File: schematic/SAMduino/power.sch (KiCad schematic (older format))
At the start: 35 parts, among them IC2 MCP1703AT-5002E_CB, IC3 NCP5501DT33RKG, J1 Barrel_Jack_Switch, J2 Conn_02x02_Odd_Even, J3 USB_B_Micro, J4 USB_B_Mini

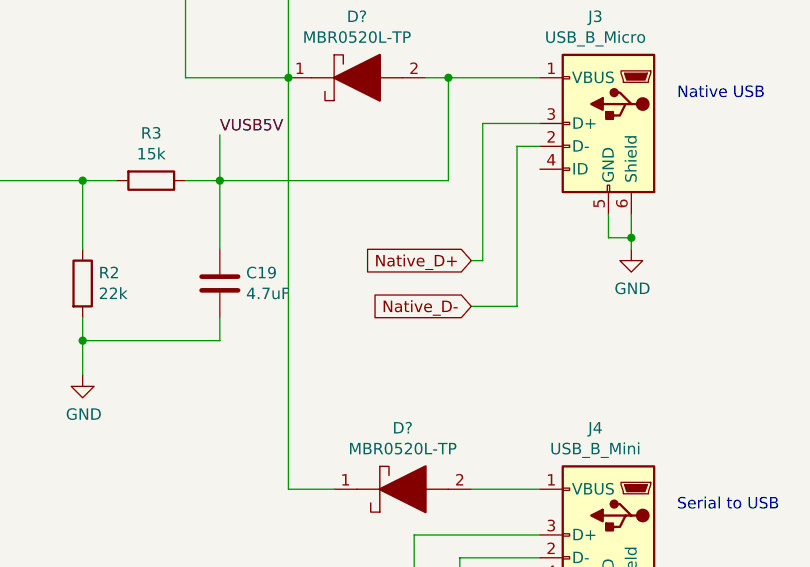
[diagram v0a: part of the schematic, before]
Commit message: Specialty pins wired
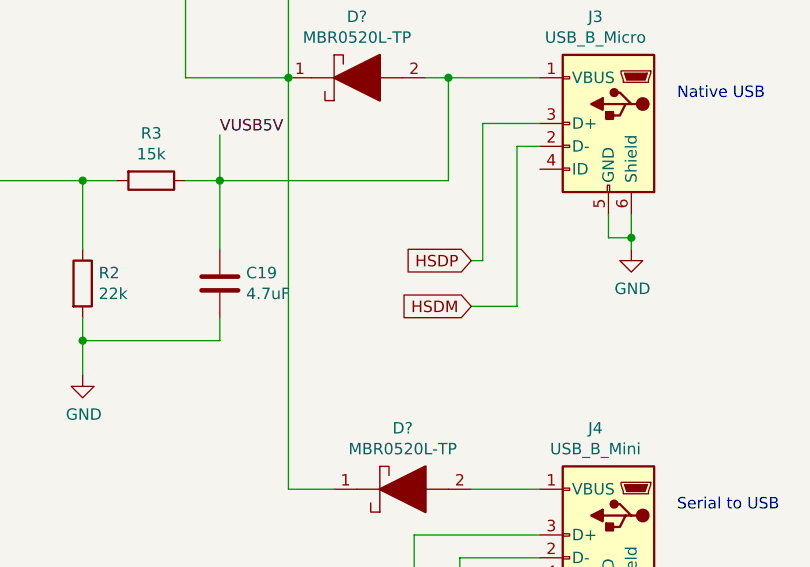
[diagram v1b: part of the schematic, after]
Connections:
- net Native_D+ renamed HSDP
- net Native_D- renamed HSDM
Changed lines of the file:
@@
 Serial_D-
 Text GLabel 7500 2250 0    50   Input ~ 0
-Native_D+
+HSDP
 Text GLabel 7500 2450 0    50   Input ~ 0
-Native_D-
+HSDM
 Wire Wire Line
 	7050 3750 7250 3750

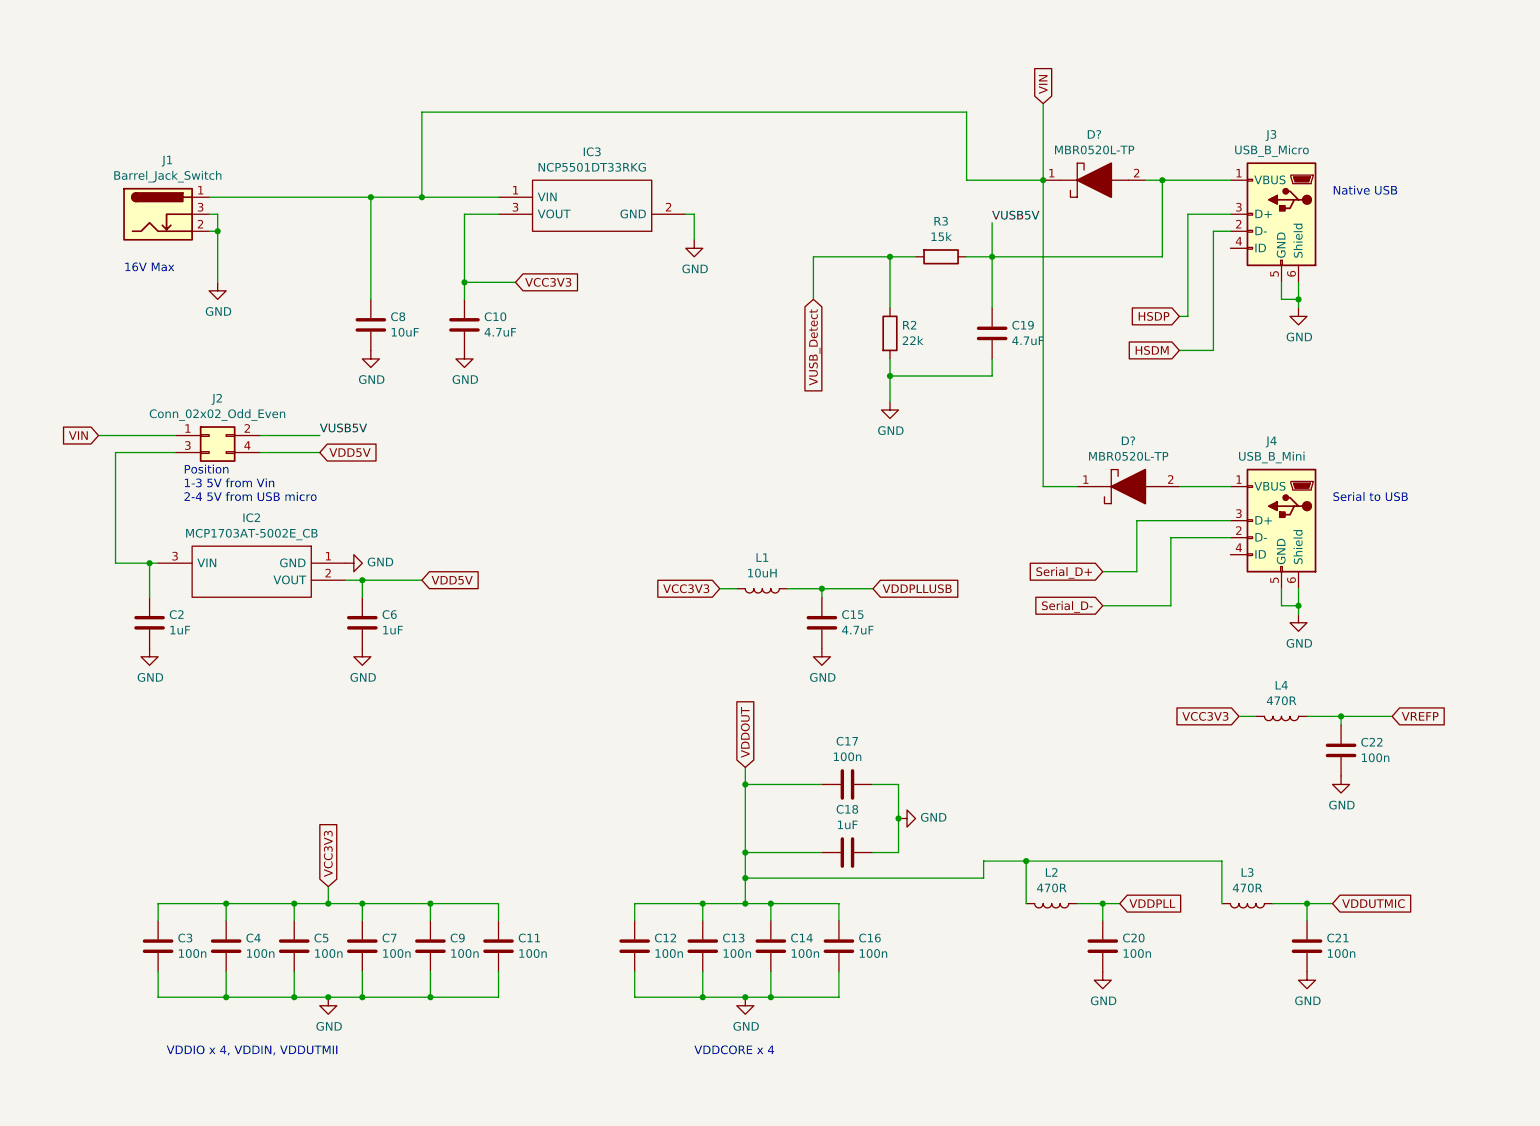
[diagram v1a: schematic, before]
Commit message: All pins connected
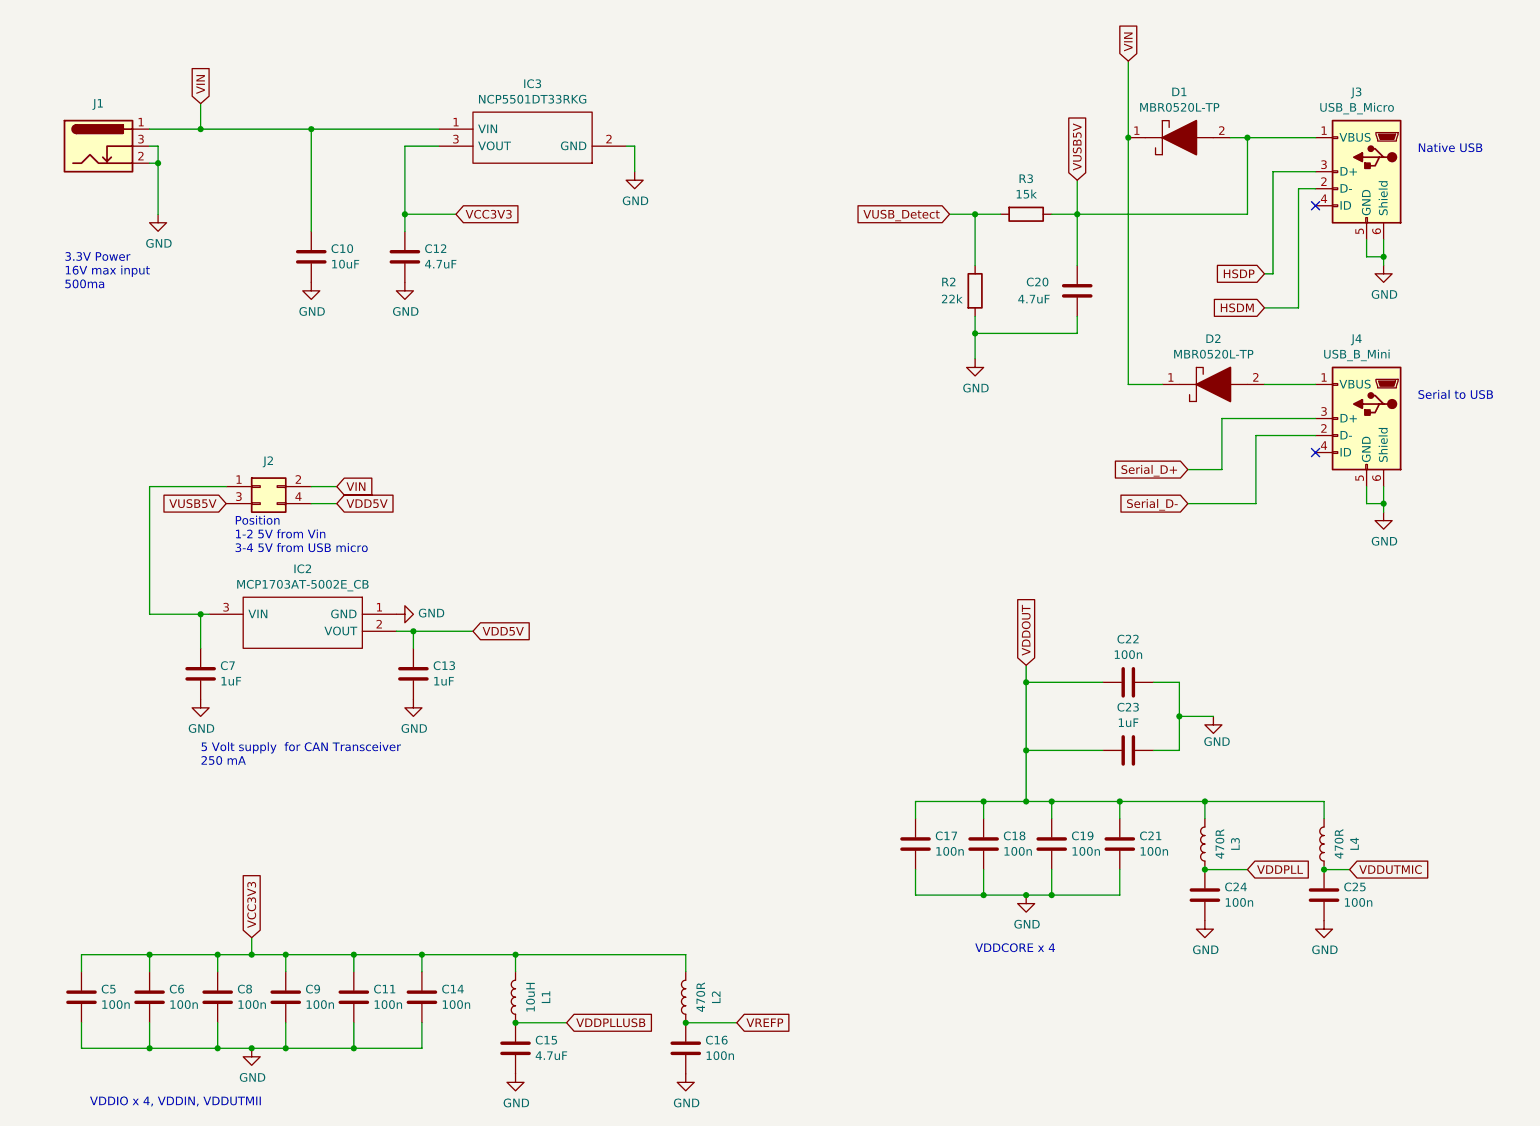
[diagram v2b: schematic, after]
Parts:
- gave numbers to parts that had none: 2
- renumbered C8 to C10, C9 to C11, C10 to C12, C6 to C13, C11 to C14, C22 to C16, C12 to C17, C13 to C18, C14 to C19, C19 to C20, C16 to C21, C17 to C22, C18 to C23, C20 to C24, C21 to C25, C3 to C5, C4 to C6, C2 to C7, C5 to C8, C7 to C9, L4 to L2, L2 to L3, L3 to L4
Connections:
- net VIN: now also J2.2 (Pin_2); no longer J2.1 (Pin_1)
- net VUSB5V: now also J2.3 (Pin_3); no longer J2.2 (Pin_2)
- net at C7.1, IC2.3 (VIN): now also J2.1 (Pin_1); no longer J2.3 (Pin_3)
- no-connect marks 0 -> 2
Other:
- note added: "3.3V Power\n16V max input\n500ma"
- note added: "5 Volt supply for CAN Transceiver\n250 mA"
- note added: "Position\n1-2 5V from Vin\n3-4 5V from USB micro"
- note removed: "16V Max"
- note removed: "Position\n1-3 5V from Vin\n2-4 5V from USB micro"
- moved on the sheet: C10, C11, C12, C13, C14, C15, C16, C17, C18, C19, C20, C21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

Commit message: Schematic with footprints
Some footprints need to be verified with actual components
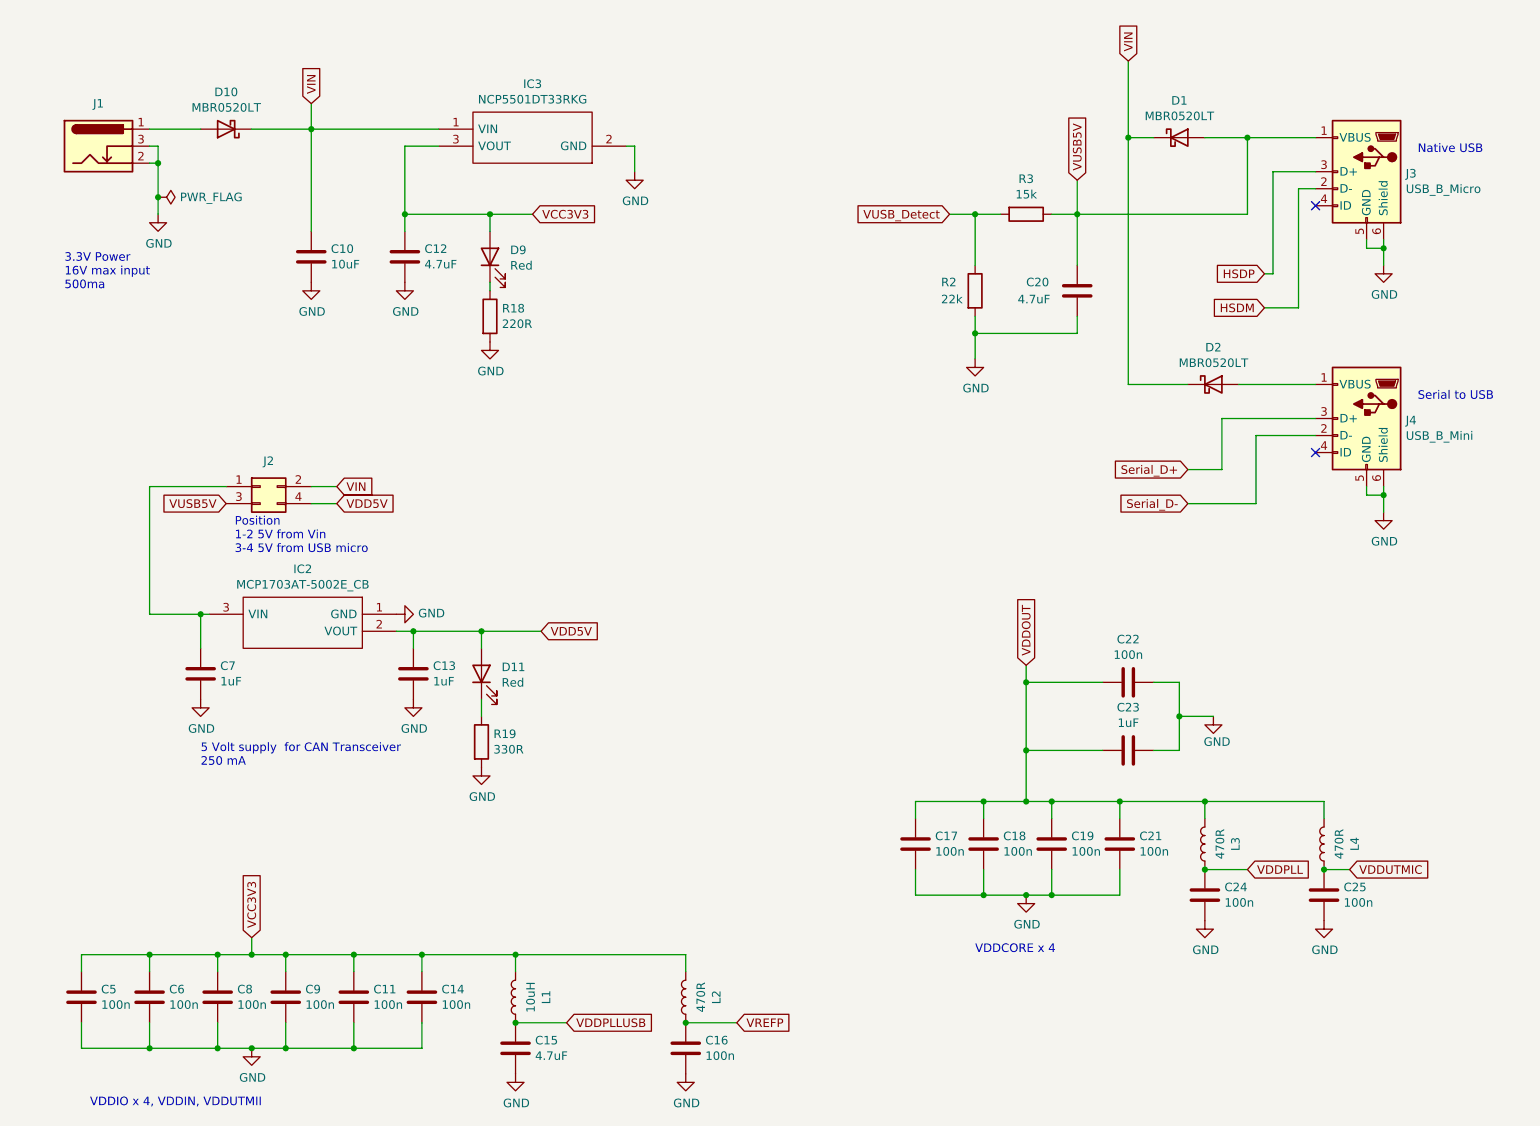
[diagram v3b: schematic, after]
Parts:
- removed D1, D2: MBR0520L-TP, SOD3716X135N, symbol SamacSys_Parts:MBR0520L-TP
- removed J3: USB_B_Micro, symbol Connector:USB_B_Micro
- removed J4: USB_B_Mini, symbol Connector:USB_B_Mini
- added D1, D10, D2: MBR0520LT, Diode_SMD:D_SOD-123, symbol Diode:MBR0520LT
- added D11, D9: Red, LED_SMD:LED_0603_1608Metric, symbol Device:LED
- added J3: USB_B_Micro, Connector_USB:USB_Micro-B_Amphenol_10104110_Horizontal, symbol SamacSys_Parts:USB_B_Micro
- added J4: USB_B_Mini, Connector_USB:USB_Mini-B_Wuerth_65100516121_Horizontal, symbol SamacSys_Parts:USB_B_Mini
- added R18: 220R, Resistor_SMD:R_0603_1608Metric, symbol Device:R
- added R19: 330R, Resistor_SMD:R_0603_1608Metric, symbol Device:R
- C10, C12, C13, C15, C20, C7: footprint (none) -> Capacitor_SMD:C_0603_1608Metric
- C11, C14, C16, C17, C18, C19, C21, C22, C23, C24, C25, C5, C6, C8, C9: footprint (none) -> Capacitor_SMD:C_0402_1005Metric
- IC2: footprint SOT95P255X145-3N -> SamacSys_Parts:SOT95P255X145-3N
- IC3: footprint NVD5117PLT4GVF01 -> SamacSys_Parts:NVD5117PLT4GVF01
- J1: footprint (none) -> Connector_BarrelJack:BarrelJack_Wuerth_6941xx301002
- J2: footprint (none) -> Connector_PinHeader_2.54mm:PinHeader_2x02_P2.54mm_Vertical
- L1, L2, L3, L4: footprint (none) -> Inductor_SMD:L_0603_1608Metric
- R2, R3: footprint (none) -> Resistor_SMD:R_0603_1608Metric
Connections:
- net GND: now also J3.5 (GND), J3.6 (Shield), J4.5 (GND), J4.6 (Shield), R18.2, R19.2
- net HSDM: now also J3.2 (D-)
- net HSDP: now also J3.3 (D+)
- net Serial_D+: now also J4.3 (D+)
- net Serial_D-: now also J4.2 (D-)
- net VCC3V3: now also D9.2 (A)
- net VDD5V: now also D11.2 (A)
- net VIN: now also D1.1 (K), D10.1 (K), D2.1 (K); no longer J1.1
- net VUSB5V: now also D1.2 (A), J3.1 (VBUS)
- new net: D10.2 (A), J1.1
- new net: D9.1 (K), R18.1
- new net: D2.2 (A), J4.1 (VBUS)
- new net: D11.1 (K), R19.1

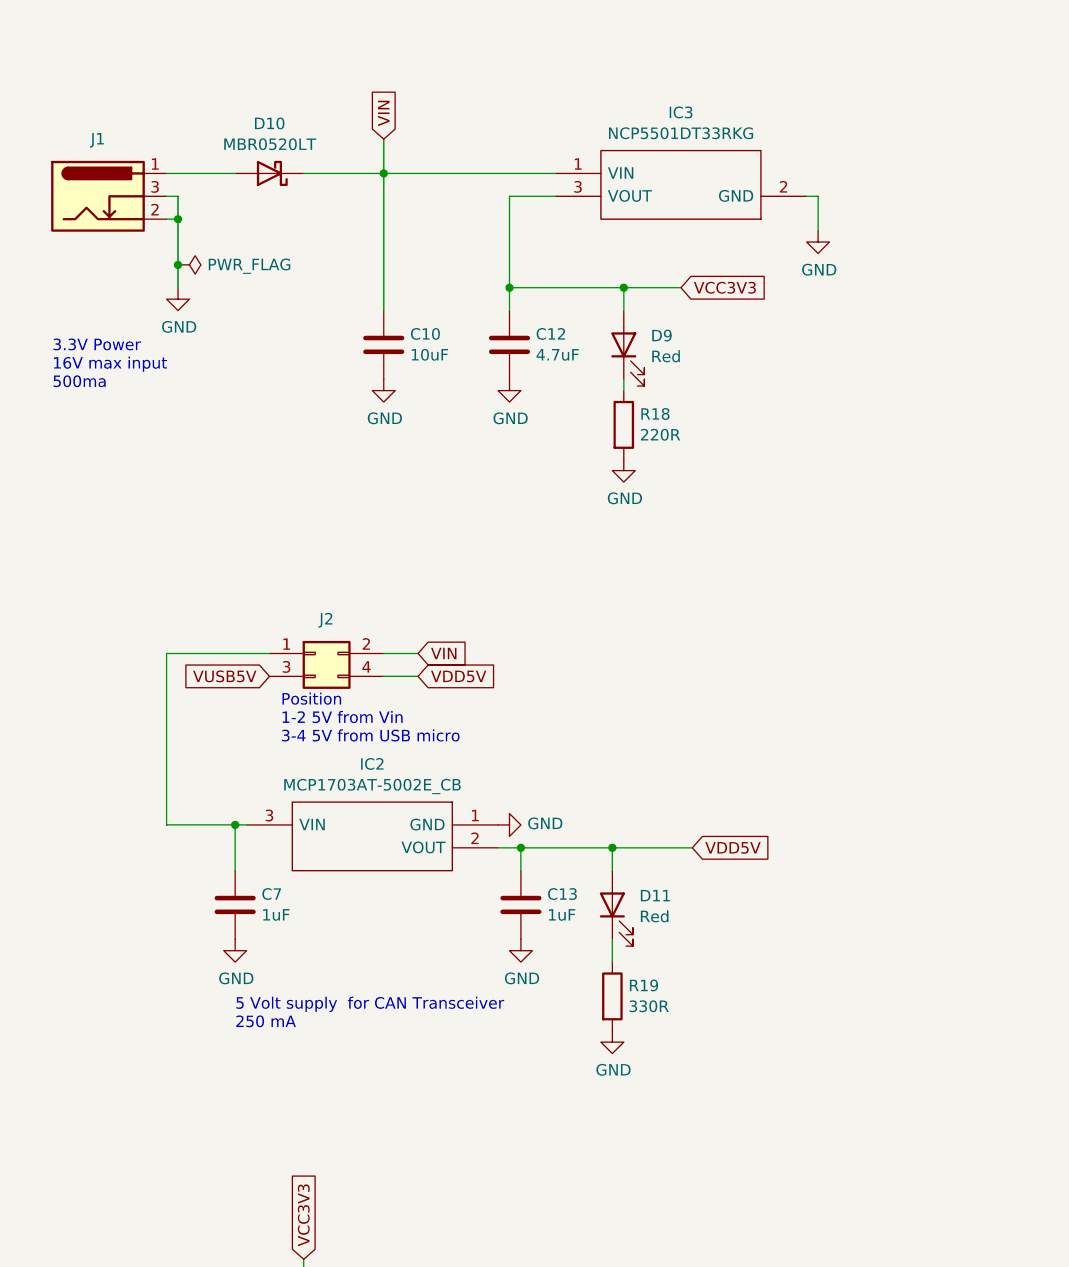
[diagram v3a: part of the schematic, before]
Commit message: Changed voltage regulators
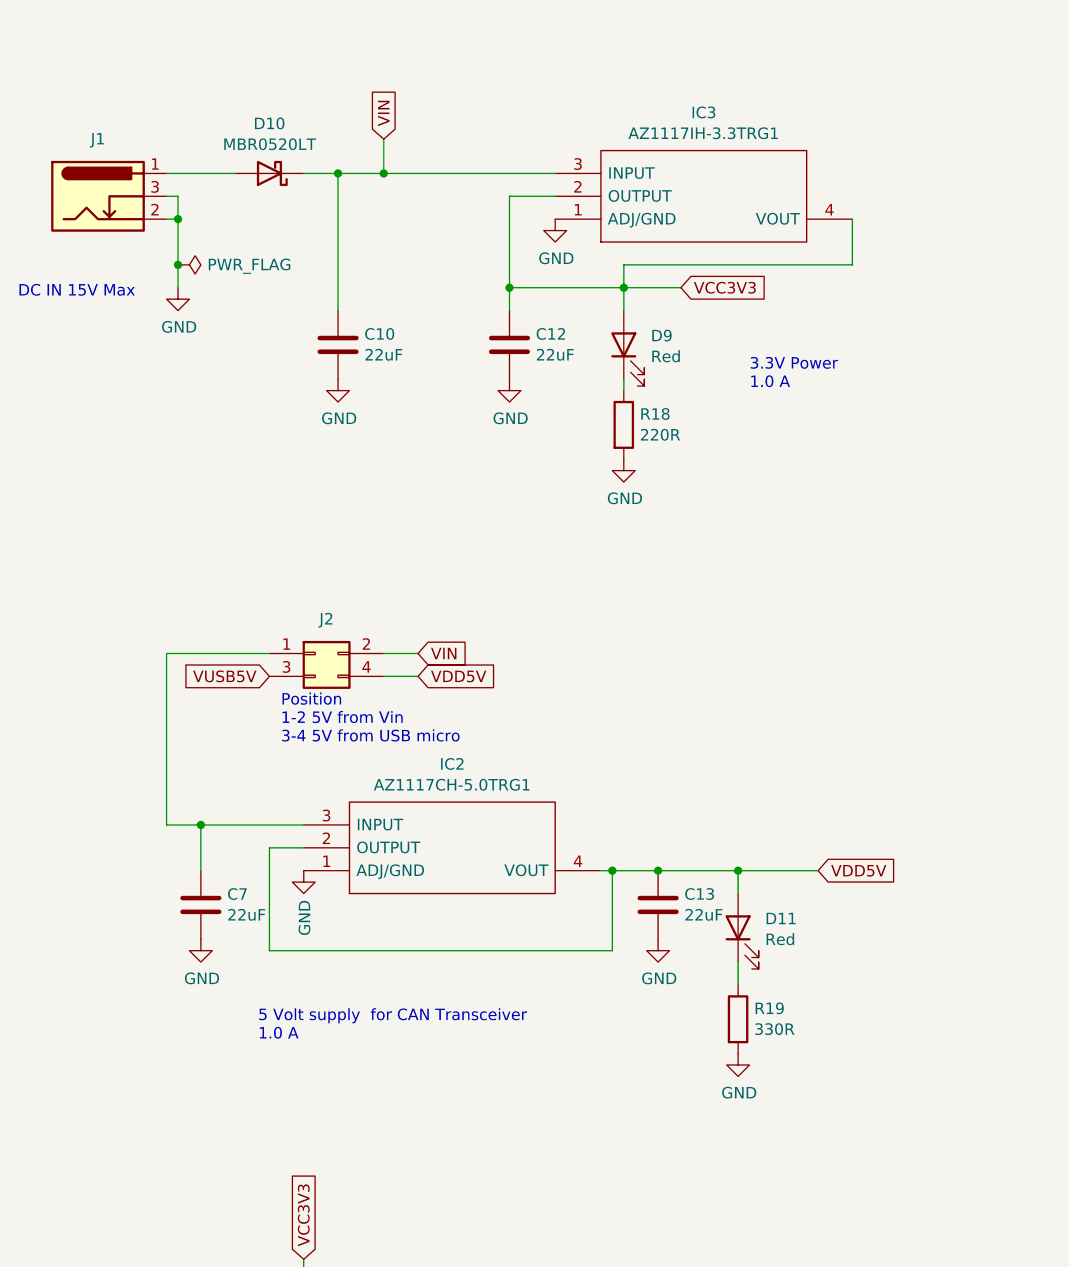
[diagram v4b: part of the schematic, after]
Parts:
- removed IC2: MCP1703AT-5002E_CB, SamacSys_Parts:SOT95P255X145-3N, symbol SamacSys_Parts:MCP1703AT-5002E_CB
- removed IC3: NCP5501DT33RKG, SamacSys_Parts:NVD5117PLT4GVF01, symbol SamacSys_Parts:NCP5501DT33RKG
- added IC2: AZ1117CH-5.0TRG1, SOT230P700X180-4N, symbol SamacSys_Parts:AZ1117CH-5.0TRG1
- added IC3: AZ1117IH-3.3TRG1, SOT230P700X180-4N, symbol SamacSys_Parts:AZ1117IH-3.3TRG1
- C10: value 10uF -> 22uF; footprint Capacitor_SMD:C_0603_1608Metric -> Capacitor_SMD:C_0805_2012Metric
- C12: value 4.7uF -> 22uF
- C13: value 1uF -> 22uF
- C7: value 1uF -> 22uF; footprint Capacitor_SMD:C_0603_1608Metric -> Capacitor_SMD:C_0805_2012Metric
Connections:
- net GND: now also IC2.1 (ADJ/GND), IC3.1 (ADJ/GND)
- net VCC3V3: now also IC3.2 (OUTPUT), IC3.4 (VOUT)
- net VDD5V: now also IC2.2 (OUTPUT), IC2.4 (VOUT)
- net VIN: now also IC3.3 (INPUT)
- net at C7.1, J2.1 (Pin_1): now also IC2.3 (INPUT)
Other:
- note added: "3.3V Power\n1.0 A"
- note added: "5 Volt supply for CAN Transceiver\n1.0 A"
- note added: "DC IN 15V Max"
- note removed: "3.3V Power\n16V max input\n500ma"
- note removed: "5 Volt supply for CAN Transceiver\n250 mA"
- moved on the sheet: C10, C13, C7, D11, R19
